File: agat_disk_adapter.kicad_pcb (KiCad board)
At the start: 2 copper layers, 53.3 x 61 mm, 18 parts, among them J1 КОНТРОЛЛЕР, J10 PIN_32, J2_A1 ИЗОТ, J2_B2 ИЗОТ, J3 IDC‐20, J4 GOTEK, J5 Питание GOTEK, J6 ВБ, J7 Джамперы, J8 ВБ2, J9 PIN_32, J9_A1 КОНТРОЛЛЕР, J9_B2 КОНТРОЛЛЕР

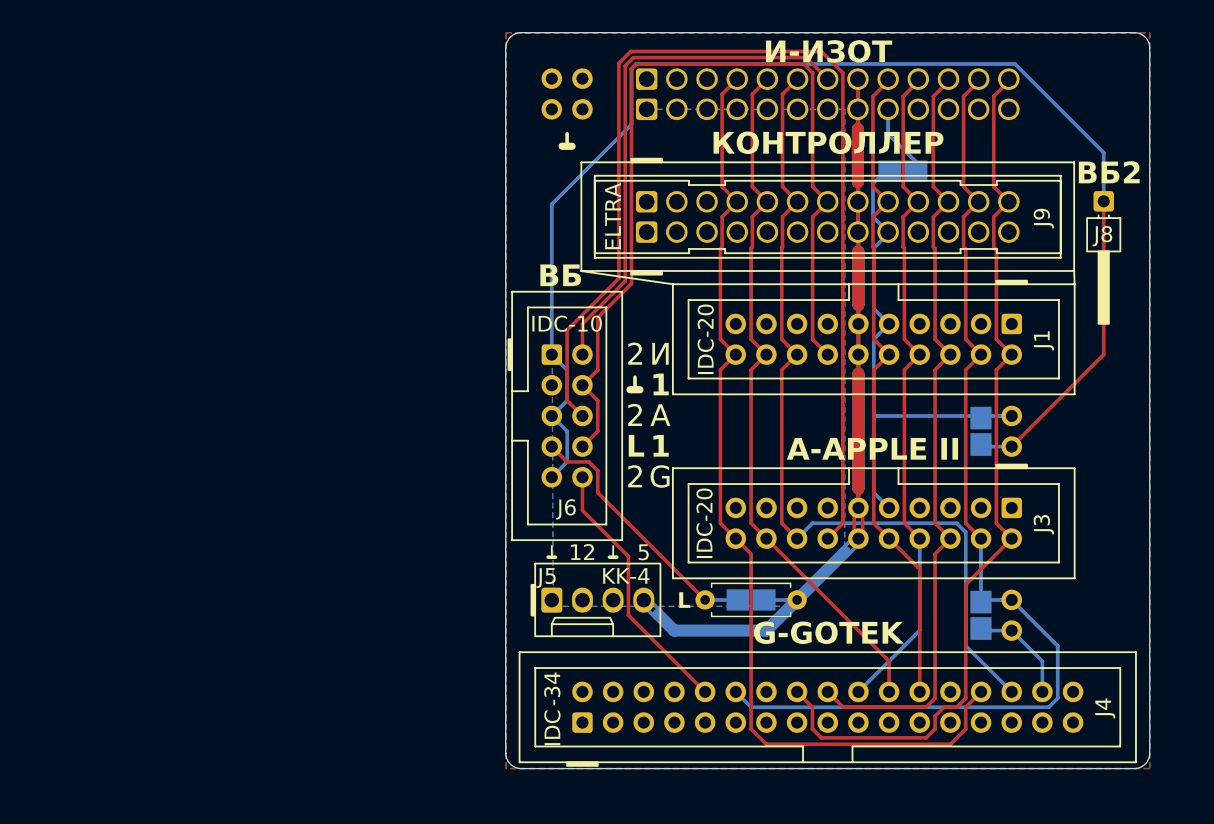
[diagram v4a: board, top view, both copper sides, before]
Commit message: create symbols and footprints for Eltras; remove unneeded solder-drops; add Agat logos
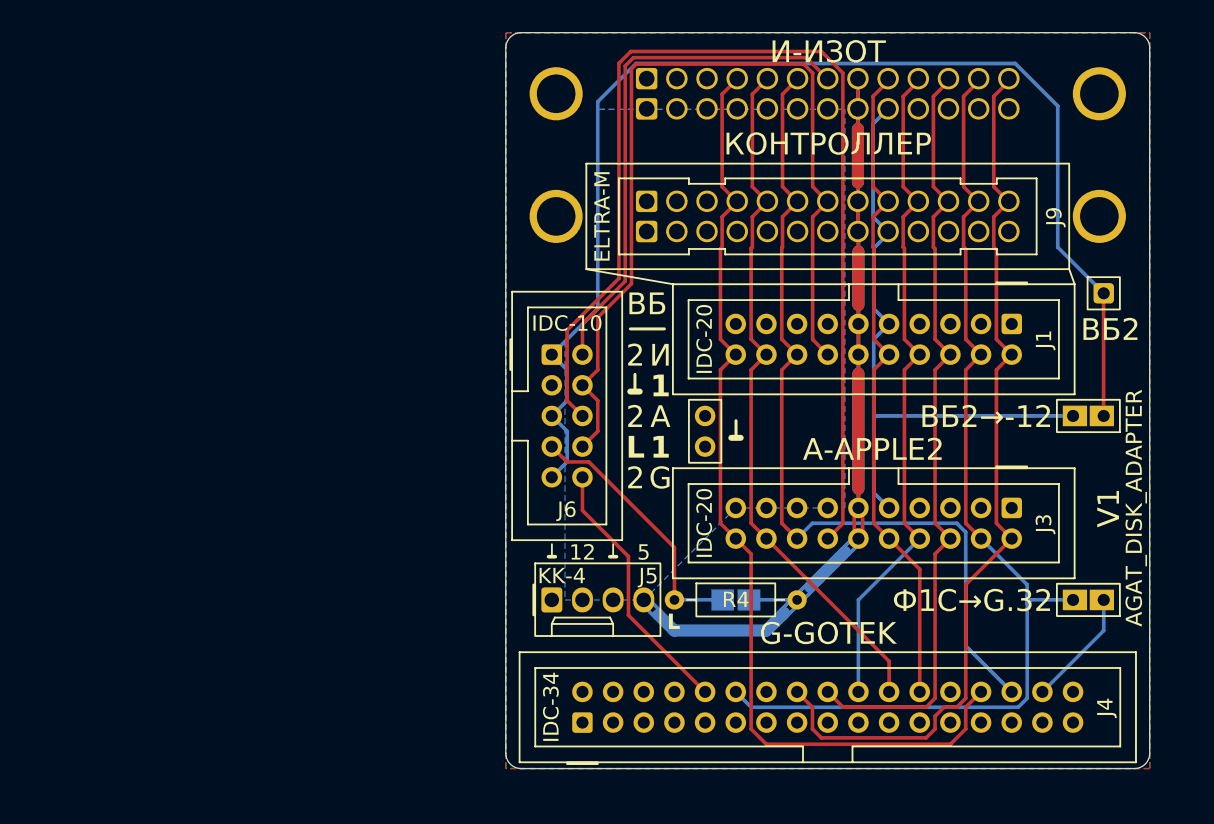
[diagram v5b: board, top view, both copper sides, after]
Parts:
- removed J2_A1, J2_B2: ИЗОТ, Connector_JST:JST_EH_B13B-EH-A_1x13_P2.50mm_Vertical
- removed J7: Джамперы, Connector_PinHeader_2.54mm:PinHeader_2x02_P2.54mm_Vertical
- removed J9_A1, J9_B2: КОНТРОЛЛЕР, Connector_JST:JST_EH_B13B-EH-A_1x13_P2.50mm_Vertical
- removed R1: 0, agat_disk_adapter:0R_1206_solder_drop_jumper
- removed R2, R3: 0R, agat_disk_adapter:0R_1206_solder_drop_jumper
- added G***: murom_museum_logo_agat_font", agat_disk_adapter:logo, F.Cu at (46.9, 40.9)
- added G***: murom_museum_logo_agat_font", agat_disk_adapter:logo, F.Cu at (46.7, 48.0)
- added G***: AGAT-LOGO-10mm-MM-INV, agat_disk_adapter:AGAT-LOGO-10mm-m-signature, F.Cu at (89.9, 48.5)
- added G***: murom_museum_logo_agat_font", agat_disk_adapter:logo, F.Cu at (90.2, 40.9)
- added G***: LOGO, agat_disk_adapter:AGAT-LOGO-10mm-m-signature, B.Cu at (47.5, 80.1)
- added J2: ELTRA‐26F, agat_disk_adapter:Eltra-26F, B.Cu at (68.6, 43.2)
- added J9: ELTRA‐26M, agat_disk_adapter:Eltra-26M, F.Cu at (68.6, 53.3)
- added JP7: PLD‐4, Connector_PinHeader_2.54mm:PinHeader_1x02_P2.54mm_Vertical, F.Cu at (58.4, 71.1)
- J1: value КОНТРОЛЛЕР -> IDC‐20; footprint Connector_IDC:IDC-Header_2x10_P2.54mm_Vertical -> agat_disk_adapter:IDC-20_header_vertical_rotation180
- J3: footprint Connector_IDC:IDC-Header_2x10_P2.54mm_Vertical -> agat_disk_adapter:IDC-20_header_vertical_rotation180
- J4: value GOTEK -> IDC‐34; footprint Connector_IDC:IDC-Header_2x17_P2.54mm_Vertical -> agat_disk_adapter:IDC-34_header_vertical_rotation0
- J5: value Питание GOTEK -> KK‐4; footprint Connector_Molex:Molex_KK-254_AE-6410-04A_1x04_P2.54mm_Vertical -> agat_disk_adapter:Molex_KK-4_vertical_rotation0
- J6: value ВБ -> IDC‐10; footprint Connector_IDC:IDC-Header_2x05_P2.54mm_Vertical -> agat_disk_adapter:IDC-10_header_vertical_rotation270
- J8: value ВБ2 -> PLS-1; footprint Connector_PinHeader_2.54mm:PinHeader_1x01_P2.54mm_Horizontal -> Connector_PinHeader_2.00mm:PinHeader_1x01_P2.00mm_Vertical
- JP10: renamed from J10; value PIN_32 -> PLS-2; footprint Connector_PinHeader_2.54mm:PinHeader_1x02_P2.54mm_Horizontal -> agat_disk_adapter:jumper_pins_solder_drop_vertical; moved to F.Cu
- JP11: renamed from J9; value PIN_32 -> PLS-2; footprint Connector_PinHeader_2.54mm:PinHeader_1x02_P2.54mm_Horizontal -> agat_disk_adapter:jumper_pins_solder_drop_vertical; moved to F.Cu
- R4: footprint Resistor_THT:R_Axial_DIN0207_L6.3mm_D2.5mm_P7.62mm_Horizontal -> Resistor_THT:R_Axial_DIN0207_L6.3mm_D2.5mm_P10.16mm_Horizontal
- R5: footprint agat_disk_adapter:0R_1206_solder_drop_jumper -> agat_disk_adapter:jumper_1206_solder_drop
- moved JP11 8.03 mm to (91.4, 86.4), turned to 180 degrees
- moved JP10 8.03 mm to (91.4, 71.1), turned to 180 degrees
- moved J8 7.62 mm to (91.4, 61.0), turned to 0 degrees
- moved R4 2.54 mm to (55.9, 86.4)
- moved R5 1.27 mm to (61.0, 86.4)
- turned J1 to 0 degrees
- turned J3 to 0 degrees
- turned J4 to 0 degrees
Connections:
- net /DE_J3 renamed /J3.DE
- net /DE_J4 renamed /J4.DE
- net /G32 renamed /J4.32
- J6 pad 2: /DE_J2 -> /J2.DE
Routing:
- net /J2.DE: track 0.00 -> 43.2 mm
- net /DE_J2: track 43.2 -> 0.00 mm
- net /-12|DE2: track 42.4 -> 52.7 mm
- net /DE2: track 111.3 -> 102.9 mm
- net Net-(J2_A1-Pin_9): track 6.27 -> 0.00 mm
- net /+5: track 104.7 -> 110.1 mm
- net /PH1: track 88.5 -> 84.7 mm
- net /J4.32: track 8.67 -> 9.72 mm
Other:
- rule pad_to_mask_clearance: 0.05 -> 0.11
- board text added: "-12|DE2"
- board text added: "20"
- board text added: "32"
- board text added: "AGAT_DISK_ADAPTER"
- board text added: "B"
- board text added: "DE"
- board text added: "DE1"
- board text added: "J4.32"
- board text added: "JP10"
- board text added: "JP11"
- board text added: "R4"
- board text added: "V1"
- board text added: "ВБ1"
- board text added: "ДЗП"
- board text added: "ДСЧ"
- board text added: "ЗЗП"
- board text added: "ЗПС"
- board text added: "КИБЕР‐МУЗЕЙ МУРОМ"
- board text added: "Ф0D"
- board text added: "Ф1C"
- board text added: "Ф2B"
- board text added: "Ф3A"
- board text removed: "-12"
- board text removed: "A-APPLE II"
- board text removed: "DE2"
- board text removed: "DE_"
- board text removed: "ELTRA"
- board text removed: "G-GOTEK"
- board text removed: "IDC"
- board text removed: "IDC‐10"
- board text removed: "IDC‐20"
- board text removed: "J5"
- board text removed: "J6"
- board text removed: "J7"
- board text removed: "J8"
- board text removed: "PH0->GOTEK.32 (fw 307)"
- board text removed: "R1"
- board text removed: "ВБ"
- board text removed: "ВБ2"
- board text removed: "И-ИЗОТ"
- board text removed: "КИБЕР‐ МУЗЕЙ МУРОМ"
- board text removed: "КОНТРОЛЛЕР"
- board text removed: "‐34"

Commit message: improve silkscreen, fix DRC issues, fix jumper holder pins connection to GND; improve schematics
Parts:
- G*** (x3): footprint agat_disk_adapter:logo -> agat_disk_adapter:murom_museum_logo_agat_font
- J2: value ELTRA‐26F -> ELTRA‐F
- J9: value ELTRA‐26M -> ELTRA‐M
- JP7: value PLD‐4 -> PLS‐2
- R5: value 680R -> 0R
- moved G*** 0.29 mm to (47.3, 79.9)
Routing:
- net /J4.DE: track 22.0 -> 31.1 mm
- net /WRP: track 80.2 -> 78.7 mm
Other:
- board text added: "AGAT DISK ADAPTER"
- board text added: "DE2"
- board text added: "J2.DE"
- board text added: "J3.DE"
- board text added: "J4.DE"
- board text added: "V1 2026"
- board text removed: "AGAT_DISK_ADAPTER"
- board text removed: "J1"
- board text removed: "J2"
- board text removed: "J3"
- board text removed: "J4"
- board text removed: "J9"
- board text removed: "JP10"
- board text removed: "JP11"
- board text removed: "R4"
- board text removed: "V1"
- board text removed: "КИБЕР‐МУЗЕЙ МУРОМ"

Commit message: refactor: rename refs for connectors and jumpers
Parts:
- renumbered J3 to J2, J4 to J3, J6 to J4, JP10 to JP1, JP11 to JP2, JP7 to JP3, R4 to R1, R5 to R2, J9 to XP1, J2 to XS1, J8 to XT1
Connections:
- net /J4.32 renamed /J3.32
- J2 pad 14: /J3.DE -> /J2.DE
- J3 pad 10: /J4.DE -> /J3.DE
- J4 pad 10: /J4.DE -> /J3.DE
- J4 pad 2: /J2.DE -> /XS1.DE
- J4 pad 6: /J3.DE -> /J2.DE
- XS1 pad B7: /J2.DE -> /XS1.DE
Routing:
- net /J3.DE: track 90.4 -> 31.1 mm
- net /J2.DE: track 43.2 -> 90.4 mm
- net /XS1.DE: track 0.00 -> 43.2 mm
- net /J4.DE: track 31.1 -> 0.00 mm
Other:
- board text added: "J3.32"
- board text added: "XS1.DE"
- board text removed: "J4.32"
- board text removed: "J4.DE"

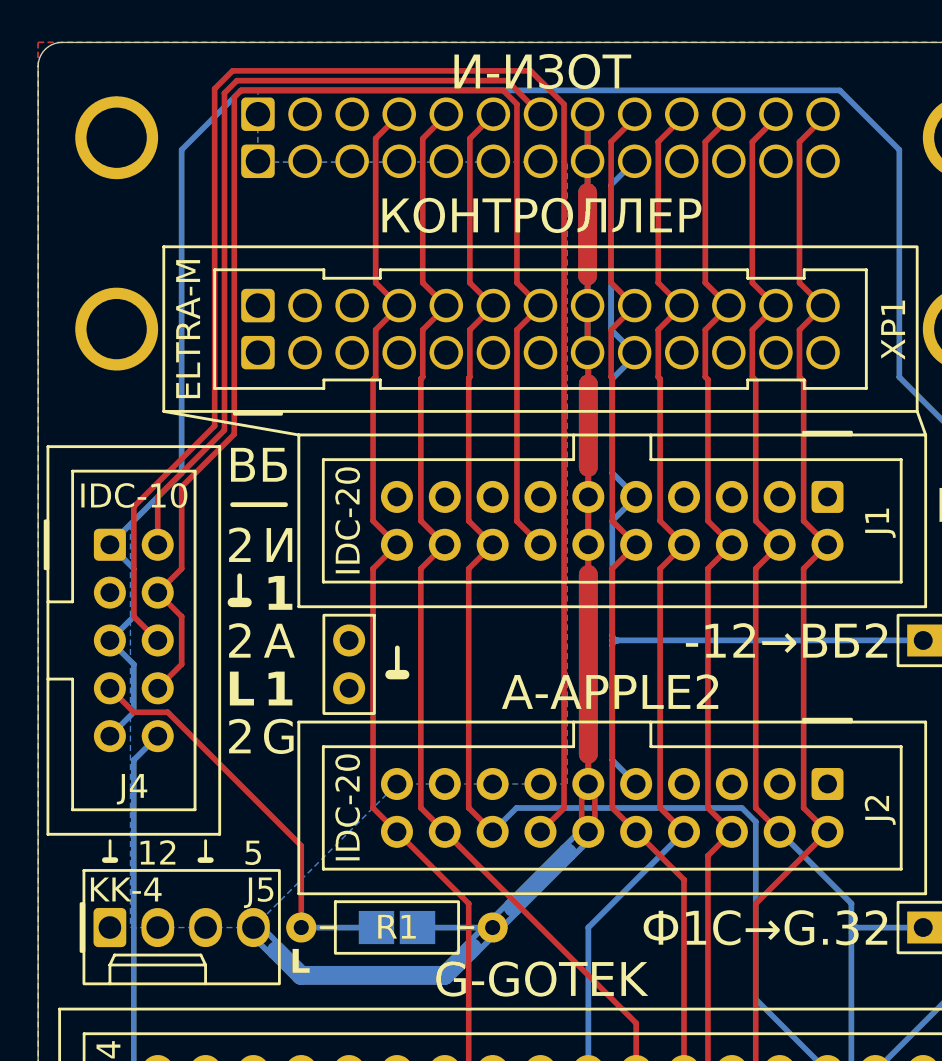
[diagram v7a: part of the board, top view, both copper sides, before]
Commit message: slightly improve pcb; fix small drc issues
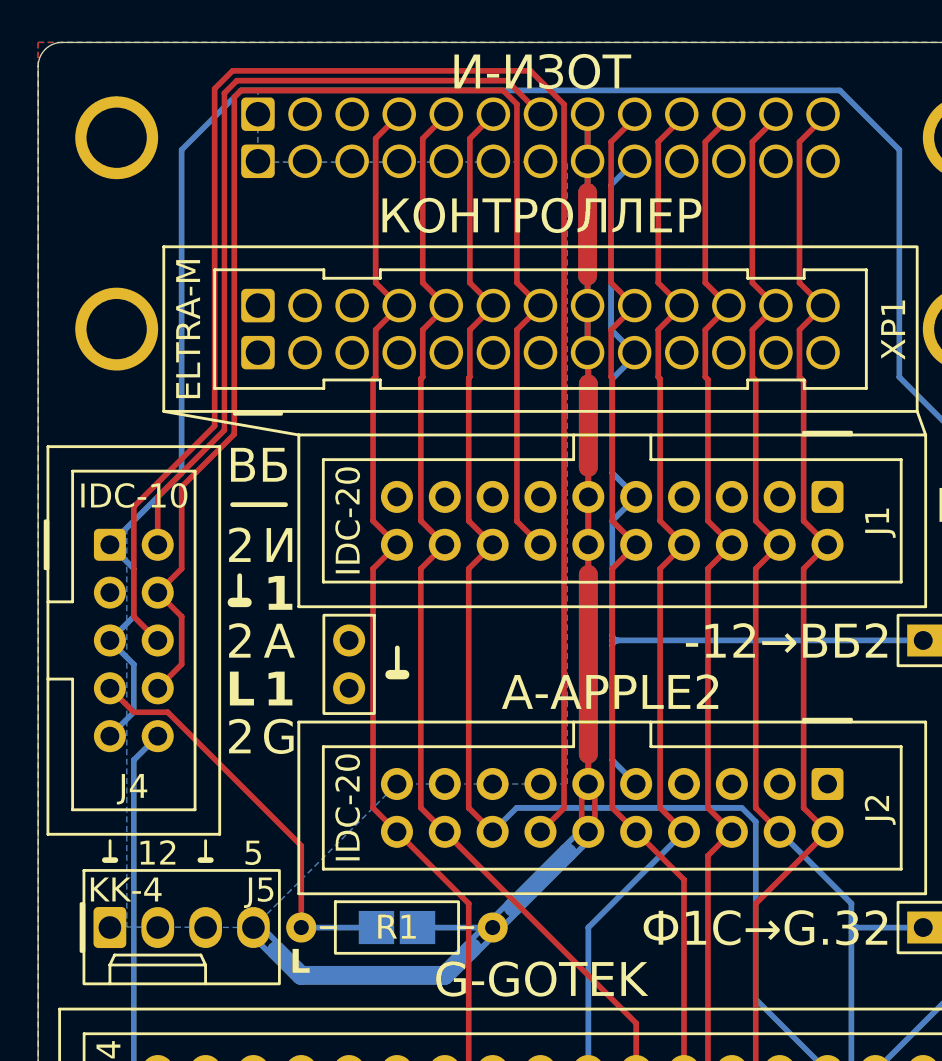
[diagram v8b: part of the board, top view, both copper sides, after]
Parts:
- JP1, JP2: value PLS-2 -> PLS‐2
- XT1: value PLS-1 -> PLS‐1
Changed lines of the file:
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@@
 		(sheetname "/")
 		(sheetfile "agat_disk_adapter.kicad_sch")
-		(units
-			(unit
-				(name "A")
-				(pins "1" "2" "3" "4")
-			)
-		)
 		(attr through_hole)
 		(duplicate_pad_numbers_are_jumpers no)
@@
 		(pad "1" thru_hole roundrect
 			(at 0 0)
-			(size 1.74 2.08)
+			(size 1.74 2.18)
 			(drill 1.2)
 			(layers "*.Cu" "*.Mask")
@@
 		(pad "2" thru_hole oval
 			(at 2.54 0)
-			(size 1.74 2.08)
+			(size 1.74 2.18)
 			(drill 1.2)
 			(layers "*.Cu" "*.Mask")
@@
 		(pad "3" thru_hole oval
 			(at 5.08 0)
-			(size 1.74 2.08)
+			(size 1.74 2.18)
 			(drill 1.2)
 			(layers "*.Cu" "*.Mask")
@@
 		(pad "4" thru_hole oval
 			(at 7.62 0)
-			(size 1.74 2.08)
+			(size 1.74 2.18)
 			(drill 1.2)
 			(layers "*.Cu" "*.Mask")
@@
 			)
 		)
-		(property "Value" "PLS-1"
+		(property "Value" "PLS‐1"
 			(at 1.01 0 0)
 			(layer "F.Fab")
@@
 			)
 		)
-		(property "Value" "PLS-2"
+		(property "Value" "PLS‐2"
 			(at 1.28 3.64 180)
 			(unlocked yes)
@@
 			)
 		)
-		(property "Value" "PLS-2"
+		(property "Value" "PLS‐2"
 			(at 1.28 3.64 180)
 			(unlocked yes)
@@
 		(sheetname "/")
 		(sheetfile "agat_disk_adapter.kicad_sch")
+		(units
+			(unit
+				(name "A")
+				(pins "SCREW_L" "B1" "A1" "B2" "A2" "B3" "A3" "B4" "A4" "B5" "A5" "B6"
+					"A6" "B7" "A7" "B8" "A8" "B9" "A9" "B10" "A10" "B11" "A11" "B12" "A12"
+					"B13" "A13" "SCREW_R"
+				)
+			)
+		)
 		(attr through_hole)
 		(duplicate_pad_numbers_are_jumpers no)
@@
 	)
 	(segment
-		(start 83.82 45.08)
-		(end 83.74 45)
-		(width 0.2)
-		(layer "F.Cu")
-		(net "GND")
-	)
-	(segment
 		(start 71.08 45.72)
 		(end 71.12 45.76)
@@
 	)
 	(segment
-		(start 71.1054 53.3546)
-		(end 71.08 53.3292)
-		(width 1.016)
-		(layer "B.Cu")
-		(net "/+5")
-	)
-	(segment
 		(start 71.12 78.74)
 		(end 71.12 77.16)
@@
 	)
 	(segment
-		(start 59.83 57.13)
-		(end 59.69 57.27)
-		(width 0.3)
-		(layer "F.Cu")
-		(net "/WRP")
-	)
-	(segment
-		(start 59.83 54.63)
-		(end 59.83 57.13)
-		(width 0.3)
-		(layer "F.Cu")
-		(net "/WRP")
-	)
-	(segment
 		(start 64.77 97.05)
 		(end 66.03 98.31)
@@
 	)
 	(segment
-		(start 59.83 52.13)
-		(end 61.08 53.38)
-		(width 0.3)
-		(layer "F.Cu")
-		(net "/WRP")
-	)
-	(segment
 		(start 60.96 66.04)
 		(end 59.69 67.31)
@@
 	(segment
 		(start 61.08 53.38)
-		(end 59.83 54.63)
+		(end 59.83 52.13)
 		(width 0.3)
 		(layer "F.Cu")
@@
 	)
 	(segment
-		(start 60.96 81.28)
-		(end 64.77 85.09)
+		(start 59.83 52.13)
+		(end 59.83 44.47)
 		(width 0.3)
 		(layer "F.Cu")
@@
 	)
 	(segment
-		(start 61.08 43.22)
-		(end 61.24 43.06)
-		(width 0.2)
-		(layer "F.Cu")
-		(net "/WRP")
-	)
-	(segment
-		(start 59.69 57.27)
-		(end 59.69 64.77)
+		(start 60.96 81.28)
+		(end 64.77 85.09)
 		(width 0.3)
 		(layer "F.Cu")
@@
 	)
 	(segment
-		(start 59.69 64.77)
-		(end 60.96 66.04)
+		(start 59.83 44.47)
+		(end 61.08 43.22)
 		(width 0.3)
 		(layer "F.Cu")
@@
 	)
 	(segment
-		(start 59.83 44.47)
-		(end 61.08 43.22)
+		(start 59.83 54.63)
+		(end 61.08 53.38)
 		(width 0.3)
 		(layer "F.Cu")
@@
 	)
 	(segment
-		(start 59.83 44.47)
-		(end 59.83 52.13)
+		(start 59.83 57.13)
+		(end 59.83 54.63)
+		(width 0.3)
+		(layer "F.Cu")
+		(net "/WRP")
+	)
+	(segment
+		(start 59.69 57.27)
+		(end 59.83 57.13)
+		(width 0.3)
+		(layer "F.Cu")
+		(net "/WRP")
+	)
+	(segment
+		(start 60.96 66.04)
+		(end 59.69 64.77)
+		(width 0.3)
+		(layer "F.Cu")
+		(net "/WRP")
+	)
+	(segment
+		(start 59.69 64.77)
+		(end 59.69 57.27)
 		(width 0.3)
 		(layer "F.Cu")
@@
 			(pts
 				(xy 70 45.72) (xy 53.58 45.72) (xy 53.58 41.92) (xy 52.681382 41.92) (xy 49.527927 45.07) (xy 49.530041 62.229959)
-				(xy 46.81 64.95) (xy 46.81 86.359994) (xy 53.34 86.36) (xy 60.96 78.74) (xy 70 78.74)
+				(xy 46.62 65.166116) (xy 46.62 86.332594) (xy 53.34 86.36) (xy 60.96 78.74) (xy 70 78.74)
 			)
 		)
